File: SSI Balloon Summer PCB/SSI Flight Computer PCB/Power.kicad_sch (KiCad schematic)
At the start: 22 parts, among them J1 Battery connector, J2 Conn_01x02, Q2 DMG2305UX-7, U11 TPS63070RNMR, U3 AP2112K-3.3TRG1

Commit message: Cleaned APRS Filter up and adding Testing points
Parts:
- added TP1, TP2, TP3, TP4: TestPoint, TestPoint:TestPoint_Pad_1.5x1.5mm, symbol Connector:TestPoint
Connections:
- net +3V3: now also TP3.1
- net +5V: now also TP1.1
- net GND: now also TP4.1
- net VBAT_PROT: now also TP2.1

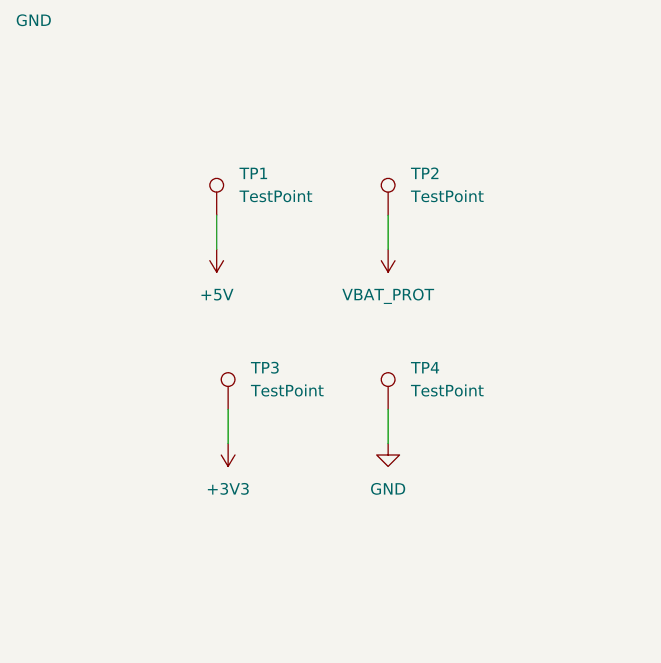
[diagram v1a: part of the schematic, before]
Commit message: Added Headers for testing, finalizing PCB
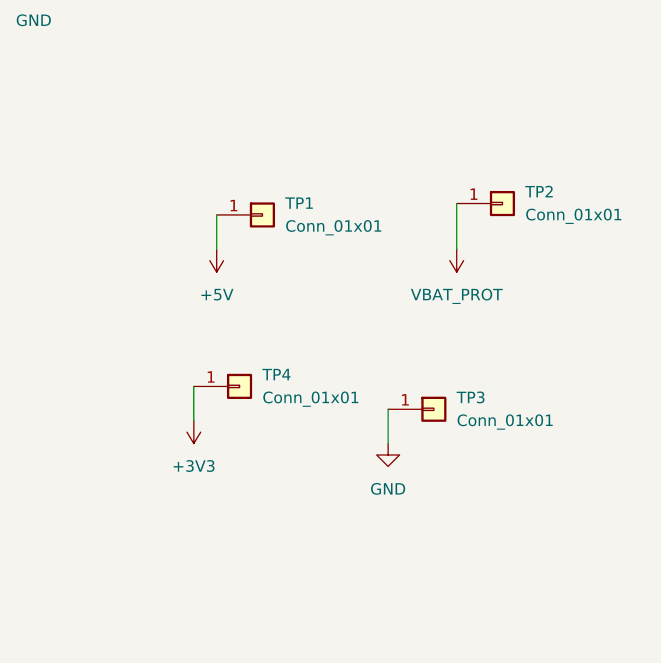
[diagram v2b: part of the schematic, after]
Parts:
- removed TP1, TP2, TP3, TP4: TestPoint, TestPoint:TestPoint_Pad_1.5x1.5mm, symbol Connector:TestPoint
- added TP1, TP2, TP3, TP4: Conn_01x01, Connector_PinHeader_2.54mm:PinHeader_1x01_P2.54mm_Vertical, symbol Connector_Generic:Conn_01x01
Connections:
- net +3V3: now also TP4.1 (Pin_1)
- net +5V: now also TP1.1 (Pin_1)
- net GND: now also TP3.1 (Pin_1)
- net VBAT_PROT: now also TP2.1 (Pin_1)

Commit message: More silkscreen organization, combined some pinheaders
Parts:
- J1: value Battery connector -> BATT_CONN
- TP1: value Conn_01x01 -> +5V
- TP2: value Conn_01x01 -> VBAT_PROT
- TP3: value Conn_01x01 -> GND
- TP4: value Conn_01x01 -> +3V3
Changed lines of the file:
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@@
 			)
 		)
-		(property "Value" "Conn_01x01"
+		(property "Value" "GND"
 			(at 222.25 113.0299 0)
 			(show_name no)
@@
 			)
 		)
-		(property "Value" "Conn_01x01"
+		(property "Value" "VBAT_PROT"
 			(at 229.87 90.1699 0)
 			(show_name no)
@@
 			)
 		)
-		(property "Value" "Battery connector"
+		(property "Value" "BATT_CONN"
 			(at 105.41 49.5299 0)
 			(show_name no)
@@
 			)
 		)
-		(property "Value" "Conn_01x01"
+		(property "Value" "+3V3"
 			(at 200.66 110.4899 0)
 			(show_name no)
@@
 			)
 		)
-		(property "Value" "Conn_01x01"
+		(property "Value" "+5V"
 			(at 203.2 91.4399 0)
 			(show_name no)

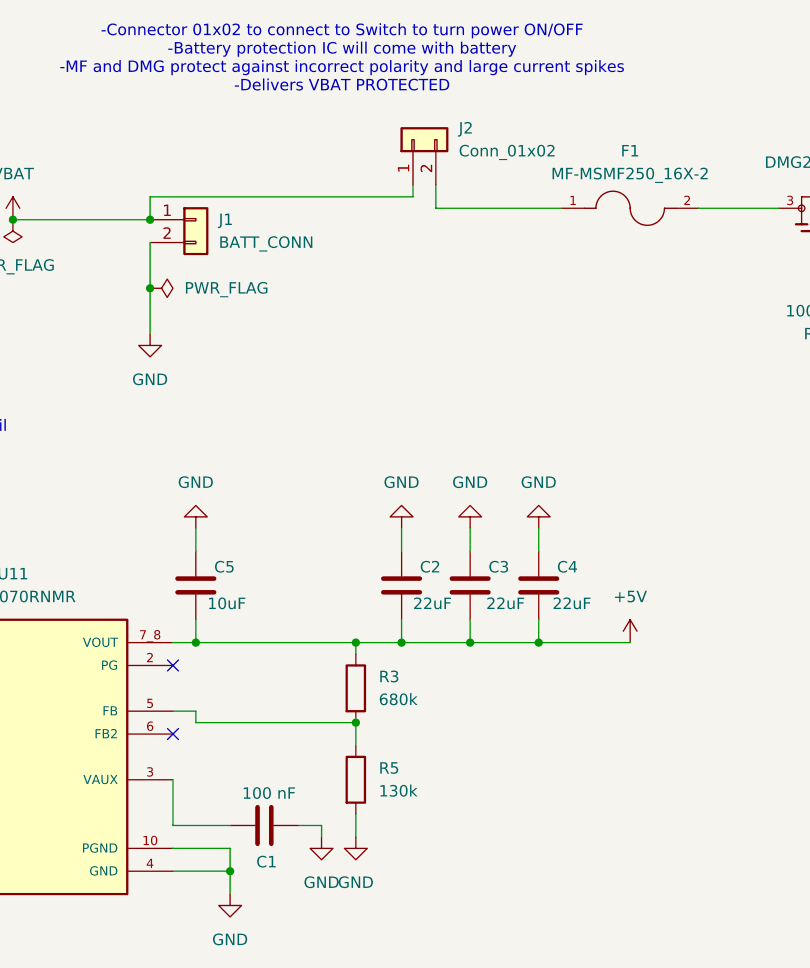
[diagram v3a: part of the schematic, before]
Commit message: finished finding all parts on JLCPCB - finalizing BOM then order
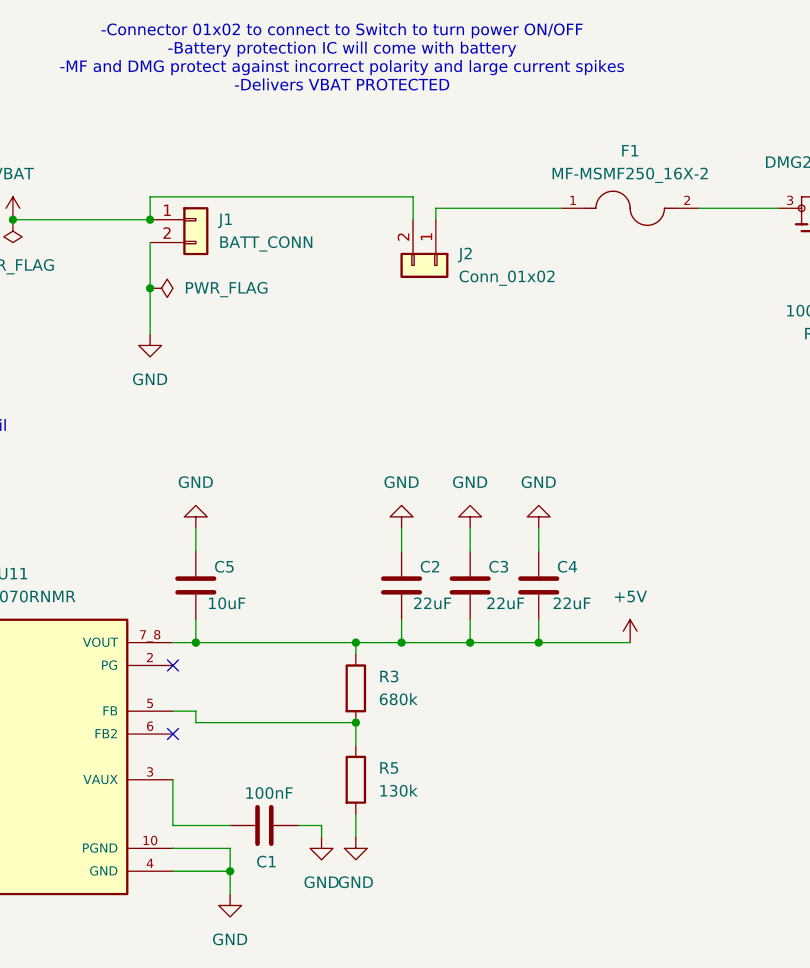
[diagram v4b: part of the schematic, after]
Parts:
- C1: value 100 nF -> 100nF; LCSC (none) -> C519438
- C10, C9: LCSC (none) -> C92806
- C2, C3, C4: LCSC (none) -> C48986262
- C5, C6: LCSC (none) -> C344022
- C7, C8: LCSC (none) -> C92009
- D2: LCSC (none) -> C2117
- F1: LCSC (none) -> C210838
- J1: LCSC (none) -> C265283
- J2: footprint Connector_JST:JST_PH_B2B-PH-K_1x02_P2.00mm_Vertical -> Connector_JST:JST_XH_B2B-XH-A_1x02_P2.50mm_Vertical; LCSC (none) -> C265283
- L1: LCSC (none) -> C18547833
- Q2: LCSC (none) -> C5261054
- R1: LCSC (none) -> C25803
- R2: LCSC (none) -> C25804
- R3: LCSC (none) -> C25822
- R5: LCSC (none) -> C22795
- TP1, TP2, TP3, TP4: LCSC (none) -> C81276
- U11: LCSC (none) -> C109322
- U3: LCSC (none) -> C51118
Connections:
- net VBAT: now also J2.2 (Pin_2); no longer J2.1 (Pin_1)
- net at F1.1: now also J2.1 (Pin_1); no longer J2.2 (Pin_2)
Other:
- moved on the sheet: J2

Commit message: PCB finally done i think and ready to order
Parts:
- C1: LCSC C519438 -> C14663
- C10, C9: LCSC C92806 -> C29936
- C7, C8: LCSC C92009 -> C15850
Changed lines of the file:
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@@
 			)
 		)
-		(property "LCSC" "C92009"
+		(property "LCSC" "C15850"
 			(at 35.56 87.63 0)
 			(hide yes)
@@
 			)
 		)
-		(property "LCSC" "C92009"
+		(property "LCSC" "C15850"
 			(at 43.18 87.63 0)
 			(hide yes)
@@
 			)
 		)
-		(property "LCSC" "C92806"
+		(property "LCSC" "C29936"
 			(at 113.03 160.02 0)
 			(hide yes)
@@
 			)
 		)
-		(property "LCSC" "C519438"
+		(property "LCSC" "C14663"
 			(at 110.49 114.3 90)
 			(hide yes)
@@
 			)
 		)
-		(property "LCSC" "C92806"
+		(property "LCSC" "C29936"
 			(at 82.55 160.02 0)
 			(hide yes)

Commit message: Board done but we have a price crisis so might have to change things
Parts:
- C2, C3, C4: LCSC C48986262 -> C45783
- C5, C6: LCSC C344022 -> C96446
- TP1, TP2, TP3, TP4: now not fitted; now left out of the parts list
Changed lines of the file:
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@@
 			)
 		)
-		(property "LCSC" "C344022"
+		(property "LCSC" "C96446"
 			(at 60.96 87.63 0)
 			(hide yes)
@@
 			)
 		)
-		(property "LCSC" "C48986262"
+		(property "LCSC" "C45783"
 			(at 125.73 87.63 0)
 			(hide yes)
@@
 		(body_style 1)
 		(exclude_from_sim no)
-		(in_bom yes)
+		(in_bom no)
 		(on_board yes)
 		(in_pos_files yes)
-		(dnp no)
+		(dnp yes)
 		(fields_autoplaced yes)
 		(property "Reference" "TP3"
@@
 		(body_style 1)
 		(exclude_from_sim no)
-		(in_bom yes)
+		(in_bom no)
 		(on_board yes)
 		(in_pos_files yes)
-		(dnp no)
+		(dnp yes)
 		(fields_autoplaced yes)
 		(property "Reference" "TP2"
@@
 			)
 		)
-		(property "LCSC" "C48986262"
+		(property "LCSC" "C45783"
 			(at 140.97 87.63 0)
 			(hide yes)
@@
 		(body_style 1)
 		(exclude_from_sim no)
-		(in_bom yes)
+		(in_bom no)
 		(on_board yes)
 		(in_pos_files yes)
-		(dnp no)
+		(dnp yes)
 		(fields_autoplaced yes)
 		(property "Reference" "TP4"
@@
 		(body_style 1)
 		(exclude_from_sim no)
-		(in_bom yes)
+		(in_bom no)
 		(on_board yes)
 		(in_pos_files yes)
-		(dnp no)
+		(dnp yes)
 		(fields_autoplaced yes)
 		(property "Reference" "TP1"
@@
 			)
 		)
-		(property "LCSC" "C344022"
+		(property "LCSC" "C96446"
 			(at 102.87 87.63 0)
 			(hide yes)
@@
 			)
 		)
-		(property "LCSC" "C48986262"
+		(property "LCSC" "C45783"
 			(at 133.35 87.63 0)
 			(hide yes)
